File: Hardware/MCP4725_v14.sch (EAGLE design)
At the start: 15 parts, among them U1 DAC_MCP4725SOT-CP

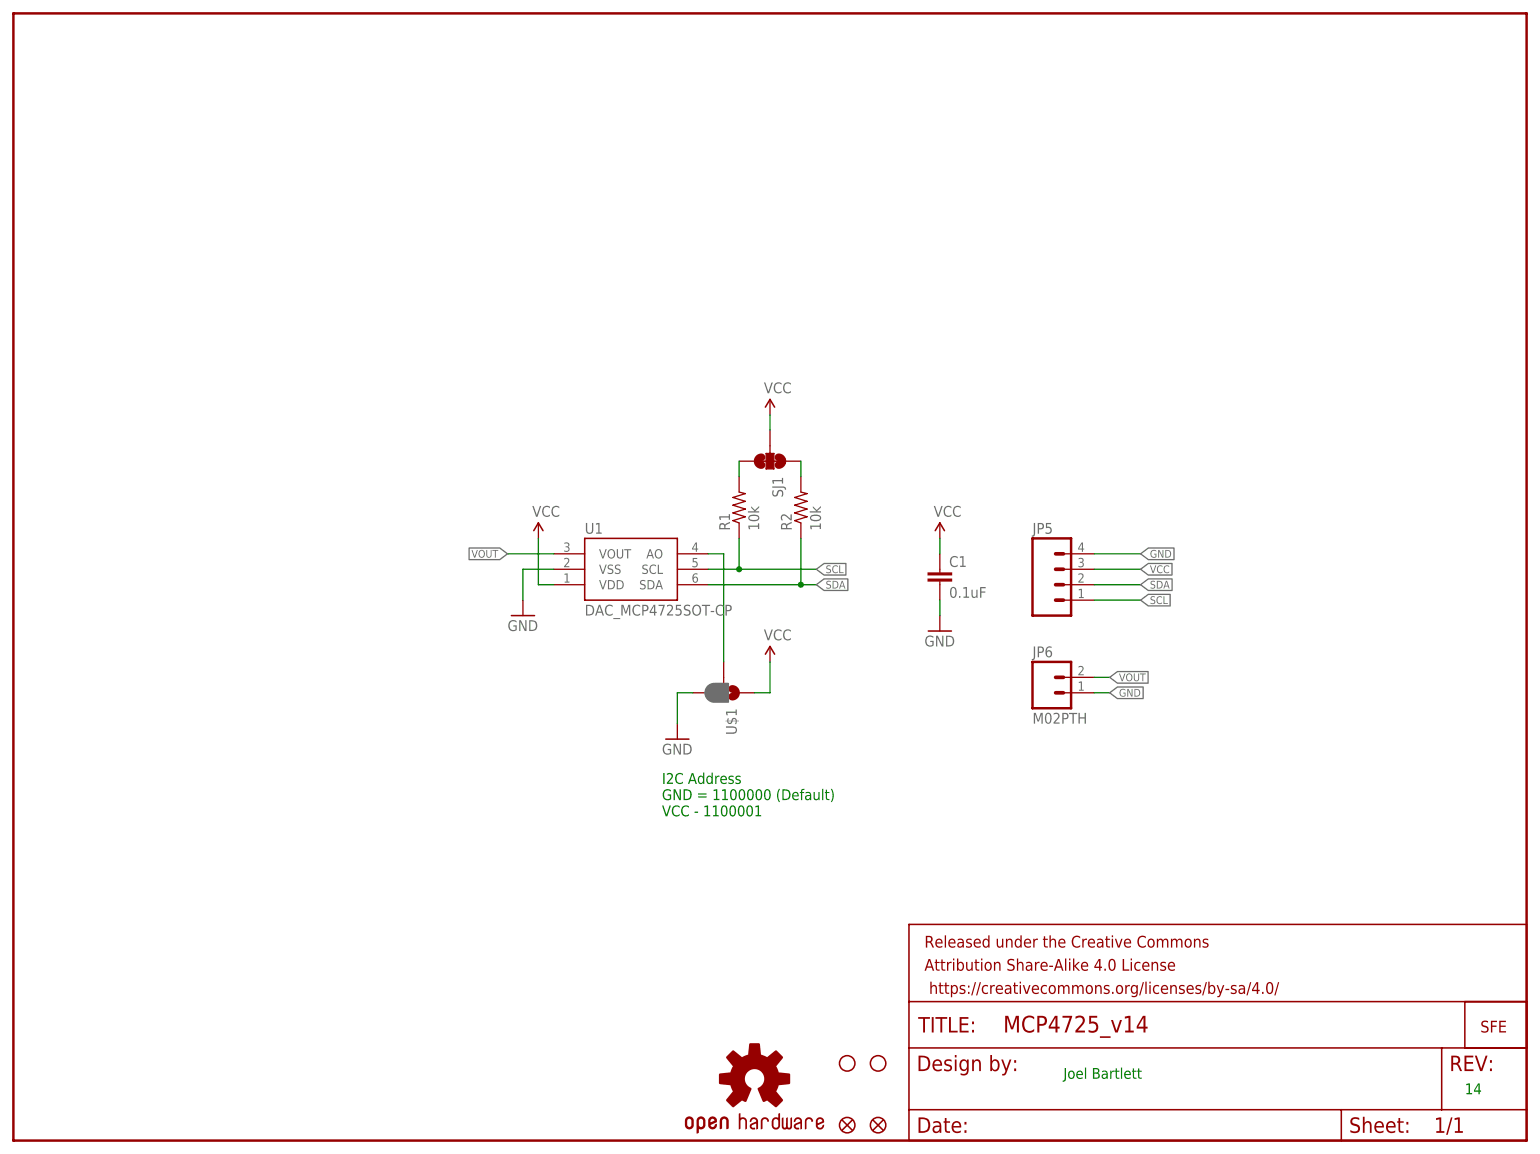
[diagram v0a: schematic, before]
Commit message: Final commit before protos
Changed 10k pull-ups to 4.7k
Added 10k to prevent shorts on I2C address selection
Added hex values for address
added name to symbol layer
clean up and organize folders
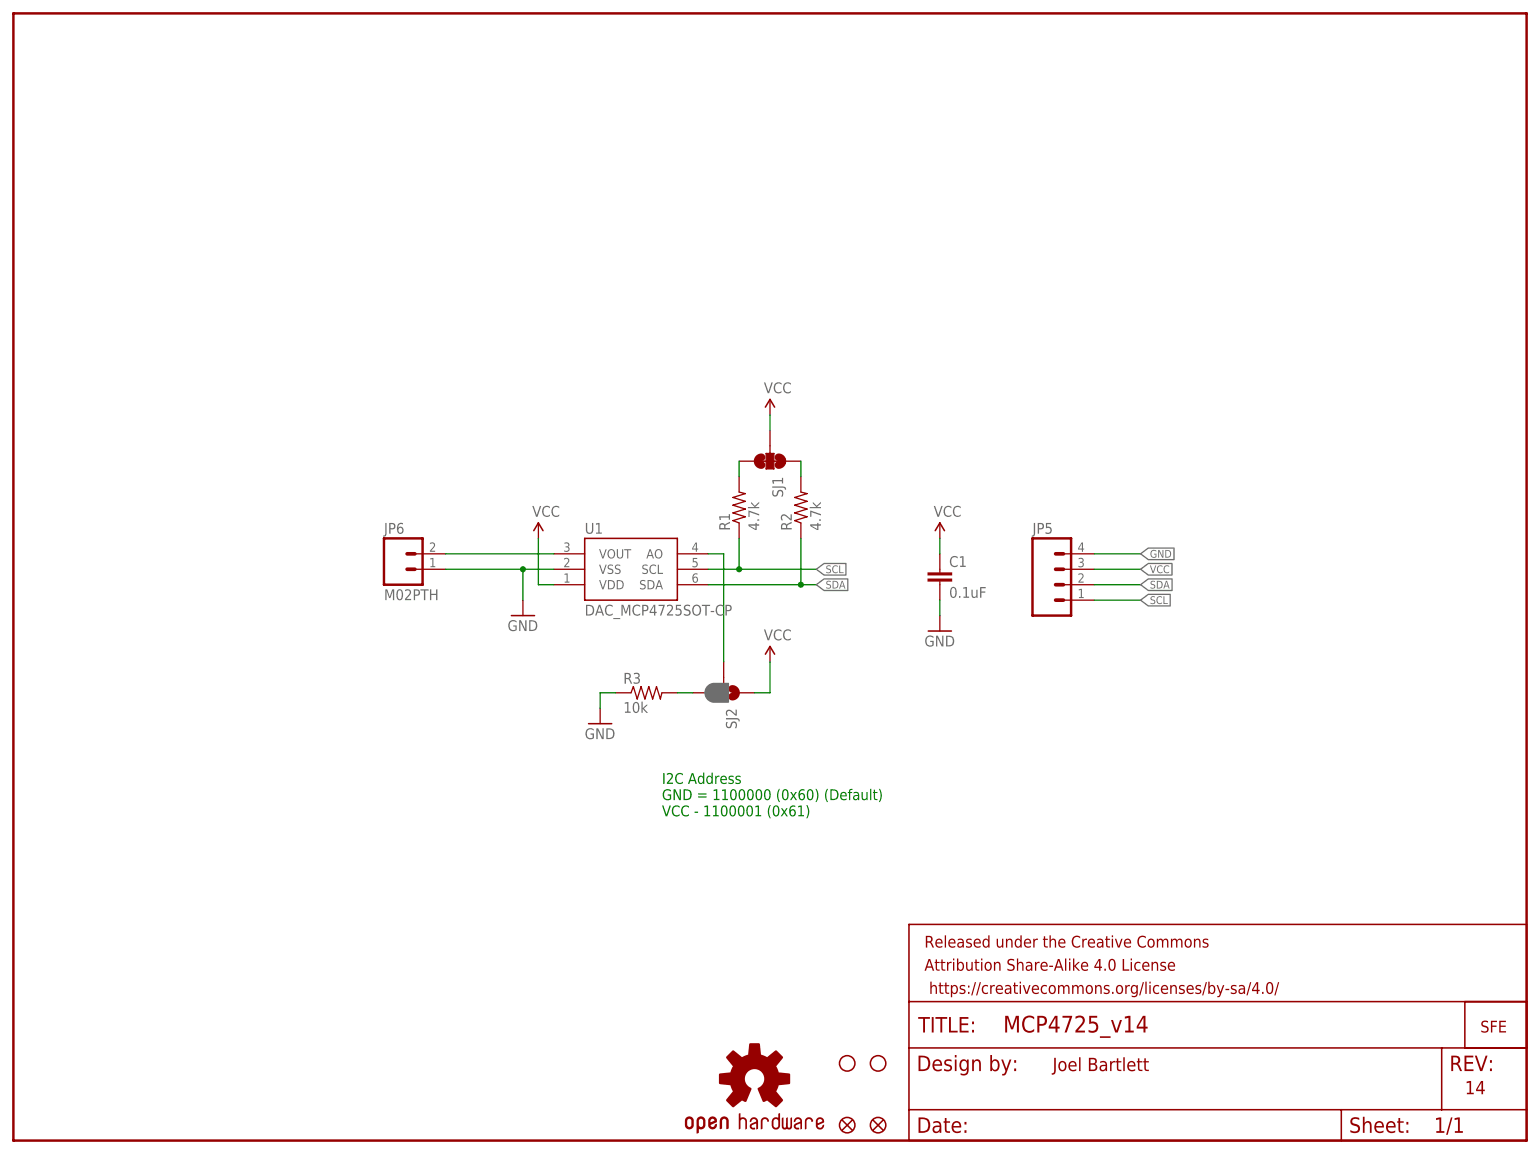
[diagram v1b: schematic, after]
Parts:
- added R3: 10k, SparkFun:RESISTOR0603-RES
- R1, R2: value 10k -> 4.7k
- renumbered U$1 to SJ2
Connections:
- new net N$4: R3.2, SJ2.3
- net GND: now also R3.1; no longer SJ2.3
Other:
- note added: "I2C Address GND = 1100000 (0x60) (Default) VCC - 1100001 (0x61)"
- note removed: "I2C Address GND = 1100000 (Default) VCC - 1100001"
- moved on the sheet: JP6
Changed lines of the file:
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@@
 <part name="GND1" library="SparkFun" deviceset="GND" device=""/>
 <part name="GND5" library="SparkFun" deviceset="GND" device=""/>
-<part name="R1" library="SparkFun" deviceset="RESISTOR" device="0603-RES" value="10k"/>
-<part name="R2" library="SparkFun" deviceset="RESISTOR" device="0603-RES" value="10k"/>
+<part name="R1" library="SparkFun" deviceset="RESISTOR" device="0603-RES" value="4.7k"/>
+<part name="R2" library="SparkFun" deviceset="RESISTOR" device="0603-RES" value="4.7k"/>
 <part name="P+2" library="SparkFun" deviceset="VCC" device=""/>
 <part name="P+4" library="SparkFun" deviceset="VCC" device=""/>
@@
 <part name="JP6" library="SparkFun-Connectors" deviceset="M02" device="PTH"/>
 <part name="SJ1" library="SparkFun-Passives" deviceset="JUMPER-PAD-3-NC_BY_TRACE" device=""/>
-<part name="U$1" library="SparkFun-Passives" deviceset="JUMPER-PAD-3-2OF3_NC_BY_PASTE" device="" value=""/>
+<part name="SJ2" library="SparkFun-Passives" deviceset="JUMPER-PAD-3-2OF3_NC_BY_PASTE" device="" value=""/>
+<part name="R3" library="SparkFun" deviceset="RESISTOR" device="0603-RES" value="10k"/>
 </parts>
 <sheets>
@@
 <plain>
 <text x="106.68" y="53.34" size="1.778" layer="91">I2C Address
-GND = 1100000 (Default)
-VCC - 1100001</text>
-<text x="172.72" y="10.16" size="1.778" layer="91">Joel Bartlett</text>
-<text x="238.76" y="7.62" size="1.778" layer="91">14</text>
+GND = 1100000 (0x60) (Default)
+VCC - 1100001 (0x61)</text>
+<text x="170.942" y="11.43" size="2.1844" layer="94">Joel Bartlett</text>
+<text x="238.76" y="7.62" size="2.1844" layer="94" ratio="9">14</text>
 </plain>
 <instances>
@@
 <instance part="JP3" gate="G$1" x="142.24" y="2.54"/>
 <instance part="U1" gate="G$1" x="101.6" y="93.98"/>
-<instance part="GND2" gate="1" x="109.22" y="66.04"/>
+<instance part="GND2" gate="1" x="96.52" y="68.58"/>
 <instance part="P+1" gate="1" x="124.46" y="78.74"/>
 <instance part="STANDOFF1" gate="G$1" x="137.16" y="12.7"/>
@@
 <instance part="LOGO1" gate="G$1" x="121.92" y="10.16"/>
 <instance part="JP5" gate="G$1" x="172.72" y="91.44"/>
-<instance part="JP6" gate="G$1" x="170.18" y="73.66"/>
+<instance part="JP6" gate="G$1" x="63.5" y="93.98"/>
 <instance part="SJ1" gate="G$1" x="124.46" y="111.76" rot="R270"/>
-<instance part="U$1" gate="G$1" x="116.84" y="73.66" rot="R270"/>
+<instance part="SJ2" gate="G$1" x="116.84" y="73.66" rot="R270"/>
+<instance part="R3" gate="G$1" x="104.14" y="73.66"/>
 </instances>
 <busses>
@@
 <pinref part="GND5" gate="1" pin="GND"/>
 <pinref part="U1" gate="G$1" pin="VSS"/>
+<pinref part="JP6" gate="G$1" pin="1"/>
+<wire x1="71.12" y1="93.98" x2="83.82" y2="93.98" width="0.1524" layer="91"/>
+<junction x="83.82" y="93.98"/>
 </segment>
 <segment>
@@
 </segment>
 <segment>
+<pinref part="R3" gate="G$1" pin="1"/>
 <pinref part="GND2" gate="1" pin="GND"/>
-<wire x1="111.76" y1="73.66" x2="109.22" y2="73.66" width="0.1524" layer="91"/>
-<wire x1="109.22" y1="73.66" x2="109.22" y2="68.58" width="0.1524" layer="91"/>
-<pinref part="U$1" gate="G$1" pin="3"/>
-</segment>
-<segment>
-<wire x1="177.8" y1="73.66" x2="180.34" y2="73.66" width="0.1524" layer="91"/>
-<label x="180.34" y="73.66" size="1.27" layer="95" xref="yes"/>
-<pinref part="JP6" gate="G$1" pin="1"/>
+<wire x1="96.52" y1="71.12" x2="96.52" y2="73.66" width="0.1524" layer="91"/>
+<wire x1="96.52" y1="73.66" x2="99.06" y2="73.66" width="0.1524" layer="91"/>
 </segment>
 </net>
@@
 <wire x1="121.92" y1="73.66" x2="124.46" y2="73.66" width="0.1524" layer="91"/>
 <wire x1="124.46" y1="73.66" x2="124.46" y2="78.74" width="0.1524" layer="91"/>
-<pinref part="U$1" gate="G$1" pin="1"/>
+<pinref part="SJ2" gate="G$1" pin="1"/>
 </segment>
 <segment>
@@
 <wire x1="116.84" y1="96.52" x2="116.84" y2="78.74" width="0.1524" layer="91"/>
 <pinref part="U1" gate="G$1" pin="AO"/>
-<pinref part="U$1" gate="G$1" pin="2"/>
+<pinref part="SJ2" gate="G$1" pin="2"/>
 </segment>
 </net>
 <net name="VOUT" class="0">
 <segment>
-<wire x1="88.9" y1="96.52" x2="81.28" y2="96.52" width="0.1524" layer="91"/>
-<label x="81.28" y="96.52" size="1.27" layer="95" rot="R180" xref="yes"/>
 <pinref part="U1" gate="G$1" pin="VOUT"/>
-</segment>
-<segment>
-<wire x1="177.8" y1="76.2" x2="180.34" y2="76.2" width="0.1524" layer="91"/>
-<label x="180.34" y="76.2" size="1.27" layer="95" xref="yes"/>
 <pinref part="JP6" gate="G$1" pin="2"/>
+<wire x1="88.9" y1="96.52" x2="71.12" y2="96.52" width="0.1524" layer="91"/>
 </segment>
 </net>
+<net name="N$4" class="0">
+<segment>
+<pinref part="SJ2" gate="G$1" pin="3"/>
+<pinref part="R3" gate="G$1" pin="2"/>
+<wire x1="109.22" y1="73.66" x2="111.76" y2="73.66" width="0.1524" layer="91"/>
+</segment>
+</net>
